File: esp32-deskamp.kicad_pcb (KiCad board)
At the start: 2 copper layers, 140.2 x 66.5 mm, 39 parts, among them J1 INPUT 00, J10 ADDITIONAL GPIO, J2 INPUT 01, J3 MUTE, J4 SLEEP, J5 PRE OUT, J6 LFE OUT, J7 INPUT SELECT, J8 MOTOR, J9 12V IN, K1 INPUT 00, K2 INPUT 01, K3 AMP MUTE, K4 AMP SLEEP, U1 ESP32 D1 MINI, U2 TSR 1-2433, U3 L9110, U4 ULN2003A

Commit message: DRC checks
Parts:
- removed ? (x6): , 
- removed the REF** at (227.2, 96.5)
- removed the REF** at (106.8, 37.2)
- removed the REF** at (227.2, 57.8)
- removed the REF** at (106.8, 96.5)
- added REF**: MountingHole_3.2mm_M3_DIN965_Pad_TopOnly, MountingHole:MountingHole_3.2mm_M3_DIN965_Pad_TopOnly, F.Cu at (227.2, 96.2)
- added REF**: MountingHole_3.2mm_M3_DIN965_Pad_TopOnly, MountingHole:MountingHole_3.2mm_M3_DIN965_Pad_TopOnly, F.Cu at (227.2, 57.5)
- added REF**: MountingHole_3.2mm_M3_DIN965_Pad_TopOnly, MountingHole:MountingHole_3.2mm_M3_DIN965_Pad_TopOnly, F.Cu at (95.8, 96.0)
- added REF**: MountingHole_3.2mm_M3_DIN965_Pad_TopOnly, MountingHole:MountingHole_3.2mm_M3_DIN965_Pad_TopOnly, F.Cu at (95.8, 38.2)
- moved J9 8.50 mm to (107.0, 39.5)
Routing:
- net +12V: track 175.0 -> 181.9 mm

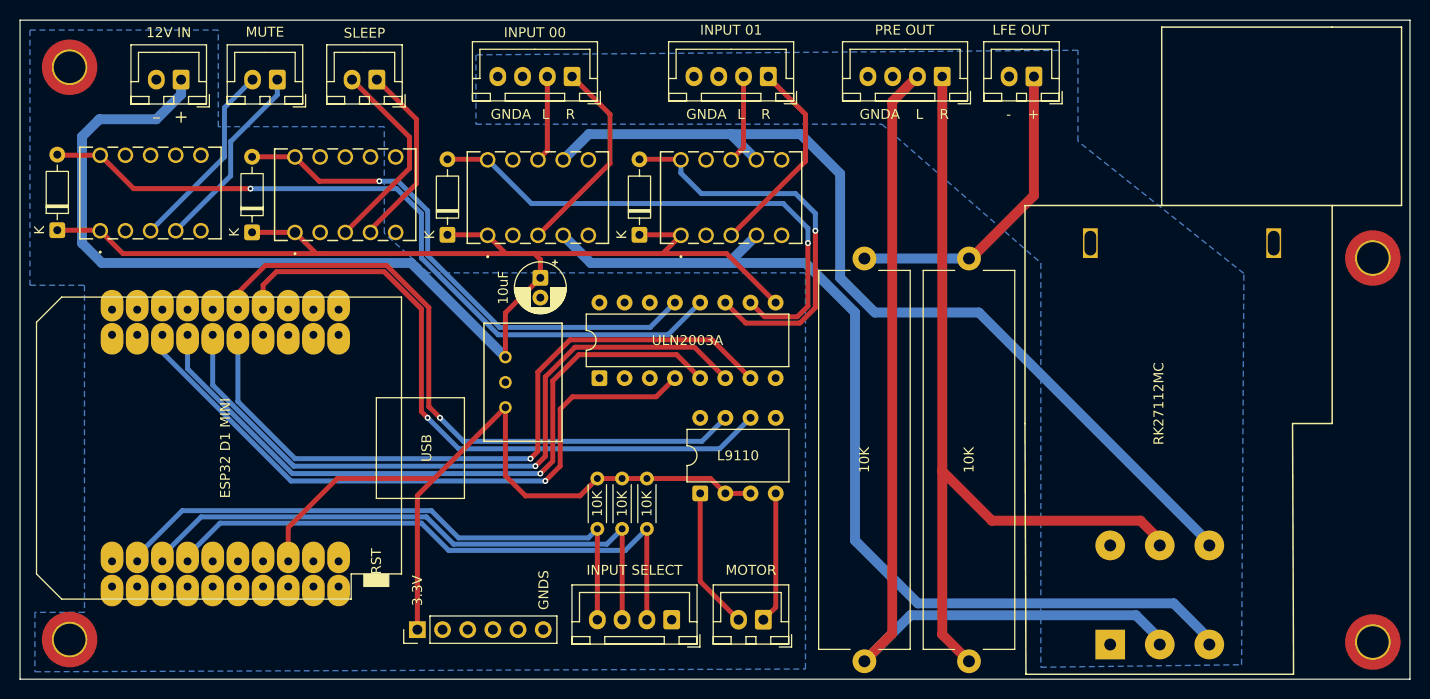
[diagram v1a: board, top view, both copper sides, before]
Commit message: Bump relays to 1mm track
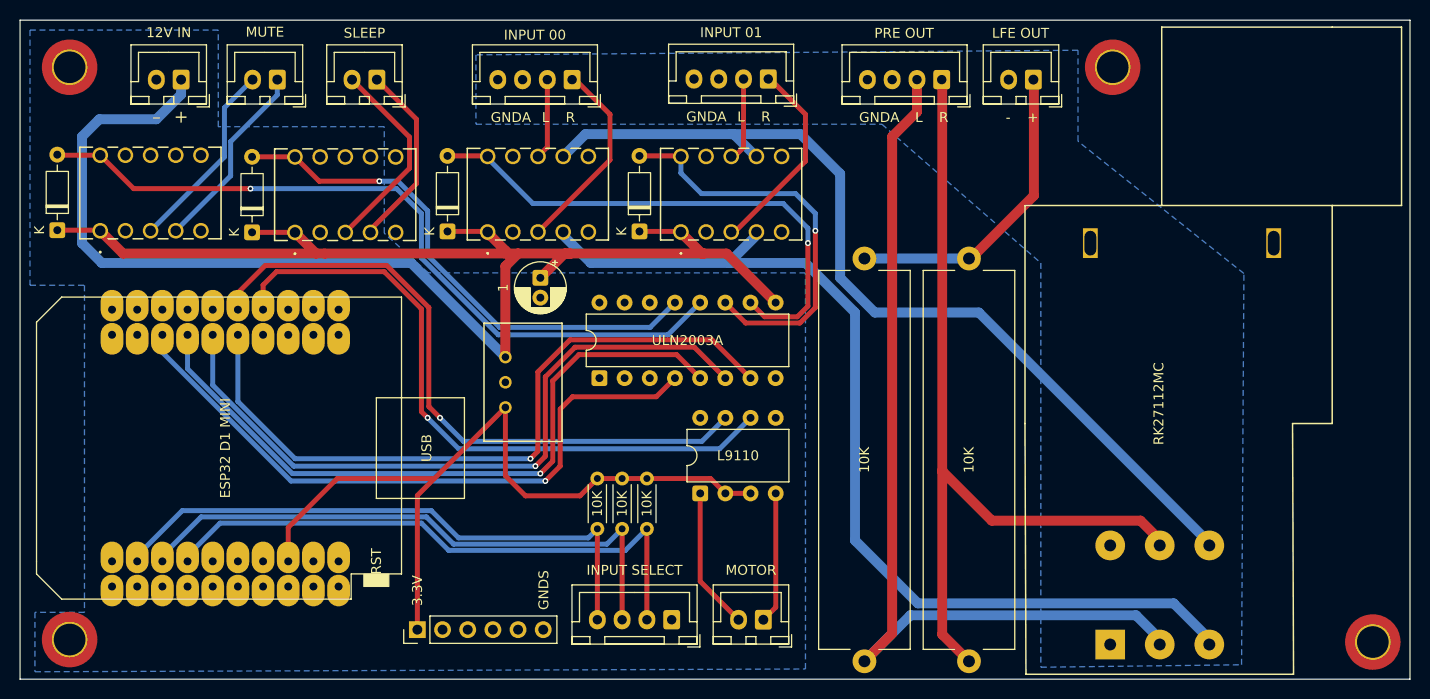
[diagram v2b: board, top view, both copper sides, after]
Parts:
- C1: value 10uF -> 1
- moved REF** 32.6 mm to (201.0, 38.2)
- moved D1 0.34 mm to (133.9, 54.8)
- moved D2 0.34 mm to (153.2, 54.8)
- moved K1 0.34 mm to (137.9, 54.9)
- moved K2 0.34 mm to (157.4, 54.9)
- moved J5 0.32 mm to (183.8, 39.5)
- moved J6 0.32 mm to (193.0, 39.5)
- moved J1 0.31 mm to (146.5, 39.5)
- moved J2 0.25 mm to (166.2, 39.4)
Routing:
- net +12V: track 181.9 -> 185.3 mm

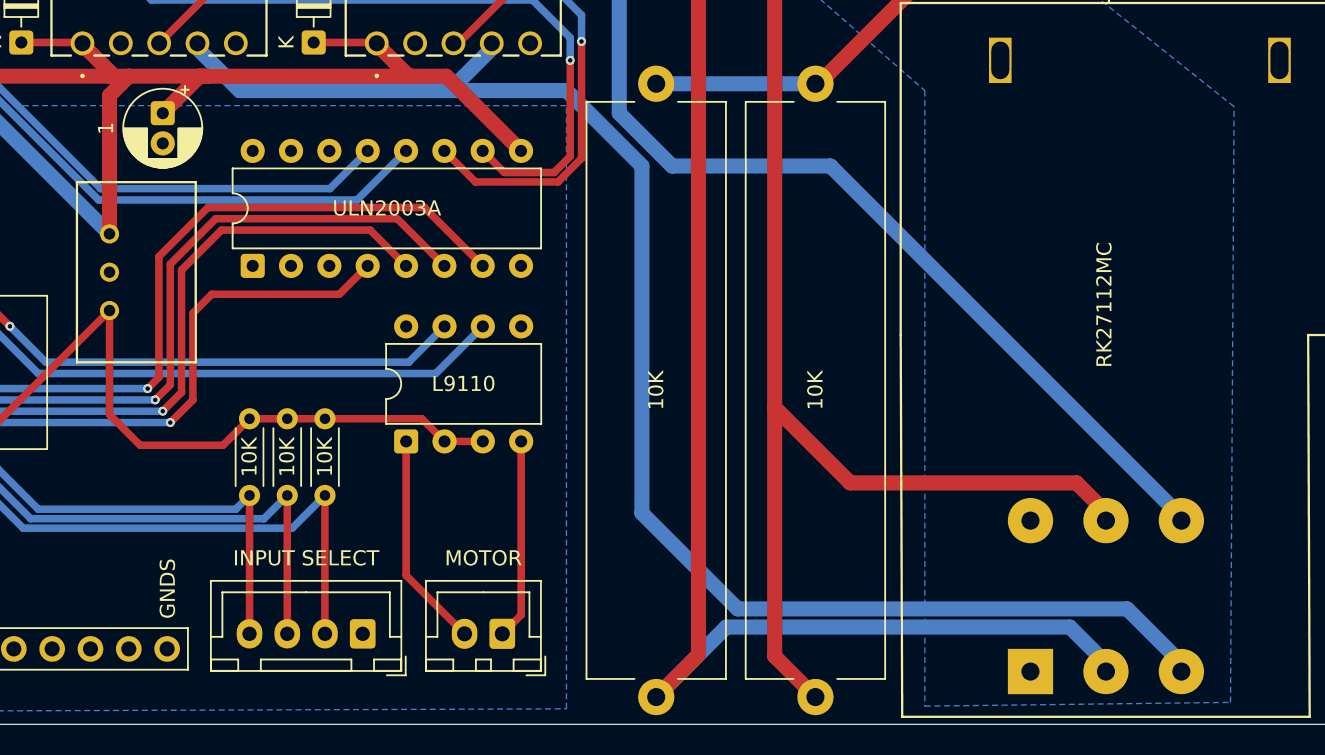
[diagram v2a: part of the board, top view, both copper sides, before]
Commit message: Name nets
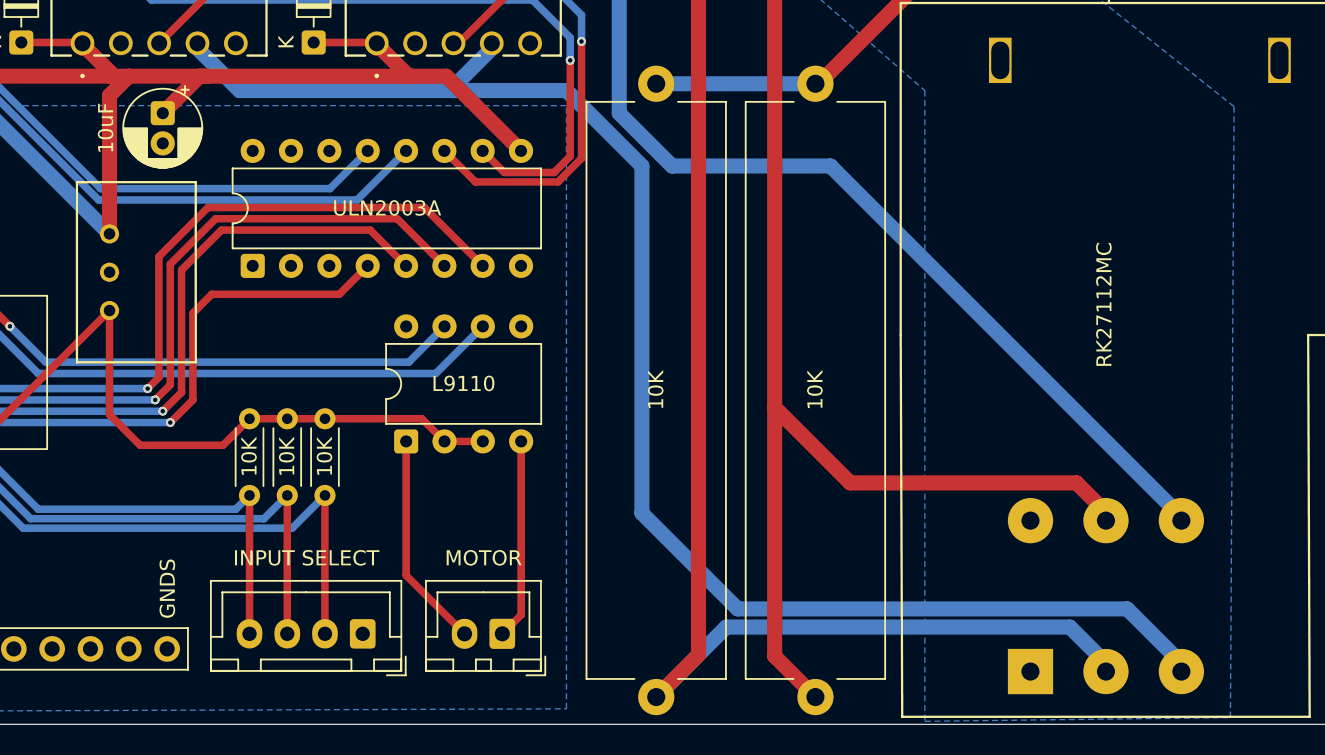
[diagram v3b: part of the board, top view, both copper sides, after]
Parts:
- C1: value 1 -> 10uF
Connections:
- J10 pad 2: unconnected-(J10-Pin_2-Pad2) -> IO1
- J10 pad 3: unconnected-(J10-Pin_3-Pad3) -> IO2
- J10 pad 4: unconnected-(J10-Pin_4-Pad4) -> IO3
- J10 pad 5: unconnected-(J10-Pin_5-Pad5) -> IO4
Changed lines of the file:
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@@
 	(net 73 "unconnected-(U1-IO_39{slash}SVN-Pad5)")
 	(net 74 "unconnected-(U1-CLK-Pad40)")
-	(net 75 "unconnected-(J10-Pin_2-Pad2)")
-	(net 76 "unconnected-(J10-Pin_4-Pad4)")
-	(net 77 "unconnected-(J10-Pin_5-Pad5)")
-	(net 78 "unconnected-(J10-Pin_3-Pad3)")
+	(net 75 "IO3")
+	(net 76 "IO2")
+	(net 77 "IO4")
+	(net 78 "IO1")
 	(net 79 "Net-(J5-Pin_1)")
 	(net 80 "Net-(J5-Pin_2)")
@@
 			)
 		)
-		(property "Value" "1"
+		(property "Value" "10uF"
 			(at 1 3.75 90)
 			(layer "F.SilkS")
@@
 			(layers "*.Cu" "*.Mask")
 			(remove_unused_layers no)
-			(net 75 "unconnected-(J10-Pin_2-Pad2)")
+			(net 78 "IO1")
 			(pinfunction "Pin_2")
 			(pintype "passive")
@@
 			(layers "*.Cu" "*.Mask")
 			(remove_unused_layers no)
-			(net 78 "unconnected-(J10-Pin_3-Pad3)")
+			(net 76 "IO2")
 			(pinfunction "Pin_3")
 			(pintype "passive")
@@
 			(layers "*.Cu" "*.Mask")
 			(remove_unused_layers no)
-			(net 76 "unconnected-(J10-Pin_4-Pad4)")
+			(net 75 "IO3")
 			(pinfunction "Pin_4")
 			(pintype "passive")
@@
 			(layers "*.Cu" "*.Mask")
 			(remove_unused_layers no)
-			(net 77 "unconnected-(J10-Pin_5-Pad5)")
+			(net 77 "IO4")
 			(pinfunction "Pin_5")
 			(pintype "passive")
@@
 		(polygon
 			(pts
-				(xy 136.75 37.000005) (xy 136.75 44) (xy 177.713636 44) (xy 193.75 58) (xy 193.75 98.793209) (xy 214.004232 98.543157)
+				(xy 136.75 37.000005) (xy 136.75 44) (xy 177.713636 44) (xy 193.75 58) (xy 193.75 99.799381) (xy 213.998207 99.549403)
 				(xy 214.240641 59.062861) (xy 197.5 45.722663) (xy 197.5 36.534488)
 			)

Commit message: Move cap
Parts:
- moved C1 1.00 mm to (144.2, 59.5)
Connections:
- J10 pad 1: +3V3 -> IO1
- J10 pad 2: IO1 -> IO2
- J10 pad 3: IO2 -> IO3
- J10 pad 4: IO3 -> IO4
- J10 pad 5: IO4 -> +3V3
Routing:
- net +3V3: track 80.1 -> 82.7 mm
- net Relay2: vias 1 -> 0
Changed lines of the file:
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@@
 	(footprint "Capacitor_THT:CP_Radial_D5.0mm_P2.00mm"
 		(layer "F.Cu")
-		(at 143.25 59.5 -90)
+		(at 144.25 59.5 -90)
 		(descr "CP, Radial series, Radial, pin pitch=2.00mm, diameter=5mm, height=7mm, Electrolytic Capacitor")
 		(tags "CP Radial series Radial pin pitch 2.00mm diameter 5mm height 7mm Electrolytic Capacitor")
@@
 			(layers "*.Cu" "*.Mask")
 			(remove_unused_layers no)
-			(net 45 "+3V3")
+			(net 78 "IO1")
 			(pinfunction "Pin_1")
 			(pintype "passive")
@@
 			(layers "*.Cu" "*.Mask")
 			(remove_unused_layers no)
-			(net 78 "IO1")
+			(net 76 "IO2")
 			(pinfunction "Pin_2")
 			(pintype "passive")
@@
 			(layers "*.Cu" "*.Mask")
 			(remove_unused_layers no)
-			(net 76 "IO2")
+			(net 75 "IO3")
 			(pinfunction "Pin_3")
 			(pintype "passive")
@@
 			(layers "*.Cu" "*.Mask")
 			(remove_unused_layers no)
-			(net 75 "IO3")
+			(net 77 "IO4")
 			(pinfunction "Pin_4")
 			(pintype "passive")
@@
 			(layers "*.Cu" "*.Mask")
 			(remove_unused_layers no)
-			(net 77 "IO4")
+			(net 45 "+3V3")
 			(pinfunction "Pin_5")
 			(pintype "passive")
@@
 	)
 	(gr_text "3.3V"
-		(at 130.84 89.5 90)
+		(at 141 89.75 90)
 		(layer "F.SilkS")
 		(effects
@@
 	)
 	(segment
+		(start 144.25 59.05)
+		(end 146.25 57.05)
+		(width 1)
+		(layer "F.Cu")
+		(net 2)
+	)
+	(segment
 		(start 145.7 57.05)
 		(end 146.25 57.05)
@@
 	)
 	(segment
+		(start 144.25 59.5)
+		(end 144.25 59.05)
+		(width 1)
+		(layer "F.Cu")
+		(net 2)
+	)
+	(segment
 		(start 98.84 54.75)
 		(end 101.14 57.05)
@@
 	)
 	(segment
-		(start 143.25 59.5)
-		(end 145.7 57.05)
-		(width 1)
-		(layer "F.Cu")
-		(net 2)
-	)
-	(segment
 		(start 138.1979 55.2131)
 		(end 139.7696 56.7848)
@@
 	)
 	(segment
-		(start 111.372 47.298)
-		(end 111.372 42.3353)
+		(start 111.872 46.798)
+		(end 111.872 41.8353)
 		(width 0.5)
-		(layer "B.Cu")
+		(layer "F.Cu")
 		(net 25)
 	)
 	(segment
-		(start 111.372 42.3353)
-		(end 114.2073 39.5)
+		(start 103.92 54.75)
+		(end 111.872 46.798)
 		(width 0.5)
-		(layer "B.Cu")
+		(layer "F.Cu")
 		(net 25)
 	)
 	(segment
-		(start 103.92 54.75)
-		(end 111.372 47.298)
+		(start 111.872 41.8353)
+		(end 114.2073 39.5)
 		(width 0.5)
-		(layer "B.Cu")
+		(layer "F.Cu")
 		(net 25)
 	)
 	(segment
-		(start 112 49.21)
-		(end 112 45.75)
+		(start 116.7073 39.5)
+		(end 112.5 43.7073)
 		(width 0.5)
-		(layer "B.Cu")
+		(layer "F.Cu")
 		(net 29)
 	)
 	(segment
-		(start 116.7073 39.5)
-		(end 116.7073 41.0427)
+		(start 106.46 53.54)
+		(end 106.46 54.75)
 		(width 0.5)
-		(layer "B.Cu")
+		(layer "F.Cu")
 		(net 29)
 	)
 	(segment
-		(start 106.46 54.75)
-		(end 112 49.21)
+		(start 112.5 47.5)
+		(end 106.46 53.54)
 		(width 0.5)
-		(layer "B.Cu")
+		(layer "F.Cu")
 		(net 29)
 	)
 	(segment
-		(start 112 45.75)
-		(end 116.7073 41.0427)
+		(start 112.5 43.7073)
+		(end 112.5 47.5)
 		(width 0.5)
-		(layer "B.Cu")
+		(layer "F.Cu")
 		(net 29)
 	)
@@
 	)
 	(segment
-		(start 130.84 95)
-		(end 130.84 81.462)
-		(width 0.5)
-		(layer "F.Cu")
-		(net 45)
-	)
-	(segment
 		(start 117.81 84.69)
 		(end 117.81 88.11)
@@
 	)
 	(segment
+		(start 141 87.75)
+		(end 149 79.75)
+		(width 0.5)
+		(layer "F.Cu")
+		(net 45)
+	)
+	(segment
 		(start 139.722 72.58)
 		(end 139.722 79.472)
@@
 	)
 	(segment
-		(start 132.552 79.75)
-		(end 130.84 81.462)
+		(start 141 95)
+		(end 141 87.75)
 		(width 0.5)
 		(layer "F.Cu")
@@
 	)
 	(segment
-		(start 114 50.5)
-		(end 102.21 50.5)
+		(start 98.84 47.13)
+		(end 94.5673 47.13)
 		(width 0.5)
 		(layer "F.Cu")
@@
 	)
 	(segment
-		(start 102.21 50.5)
-		(end 98.84 47.13)
+		(start 159.37 62)
+		(end 156.12 65.25)
 		(width 0.5)
-		(layer "F.Cu")
+		(layer "B.Cu")
 		(net 88)
 	)
 	(segment
-		(start 98.84 47.13)
-		(end 94.5673 47.13)
+		(start 156.12 65.25)
+		(end 139 65.25)
 		(width 0.5)
-		(layer "F.Cu")
-		(net 88)
-	)
-	(via
-		(at 114 50.5)
-		(size 0.6)
-		(drill 0.3)
-		(layers "F.Cu" "B.Cu")
+		(layer "B.Cu")
 		(net 88)
 	)
 	(segment
-		(start 114 50.5)
-		(end 128.75 50.5)
+		(start 139 65.25)
+		(end 131.25 57.5)
 		(width 0.5)
 		(layer "B.Cu")
@@
 	(segment
 		(start 128.75 50.5)
-		(end 131.25 53)
+		(end 102.21 50.5)
 		(width 0.5)
 		(layer "B.Cu")
@@
 	(segment
 		(start 131.25 57.5)
-		(end 139 65.25)
-		(width 0.5)
-		(layer "B.Cu")
-		(net 88)
-	)
-	(segment
-		(start 139 65.25)
-		(end 156.12 65.25)
+		(end 131.25 53)
 		(width 0.5)
 		(layer "B.Cu")
@@
 	)
 	(segment
-		(start 156.12 65.25)
-		(end 159.37 62)
+		(start 131.25 53)
+		(end 128.75 50.5)
 		(width 0.5)
 		(layer "B.Cu")
@@
 	)
 	(segment
-		(start 131.25 53)
-		(end 131.25 57.5)
+		(start 102.21 50.5)
+		(end 98.84 47.13)
 		(width 0.5)
 		(layer "B.Cu")
@@
 			(pts
 				(xy 91.75 34.5) (xy 91.75 60.25) (xy 97.25 60.25) (xy 97.25 93.25) (xy 92.25 93.25) (xy 92.25 99.25)
-				(xy 170 98.969772) (xy 170 59) (xy 131.944445 59) (xy 127.5 55) (xy 127.5 44.25) (xy 110.75 44.25)
+				(xy 170 98.969772) (xy 170 59) (xy 131.944445 59) (xy 127.5 55) (xy 127.5 51.25) (xy 110.75 51.25)
 				(xy 110.75 34.5)
 			)

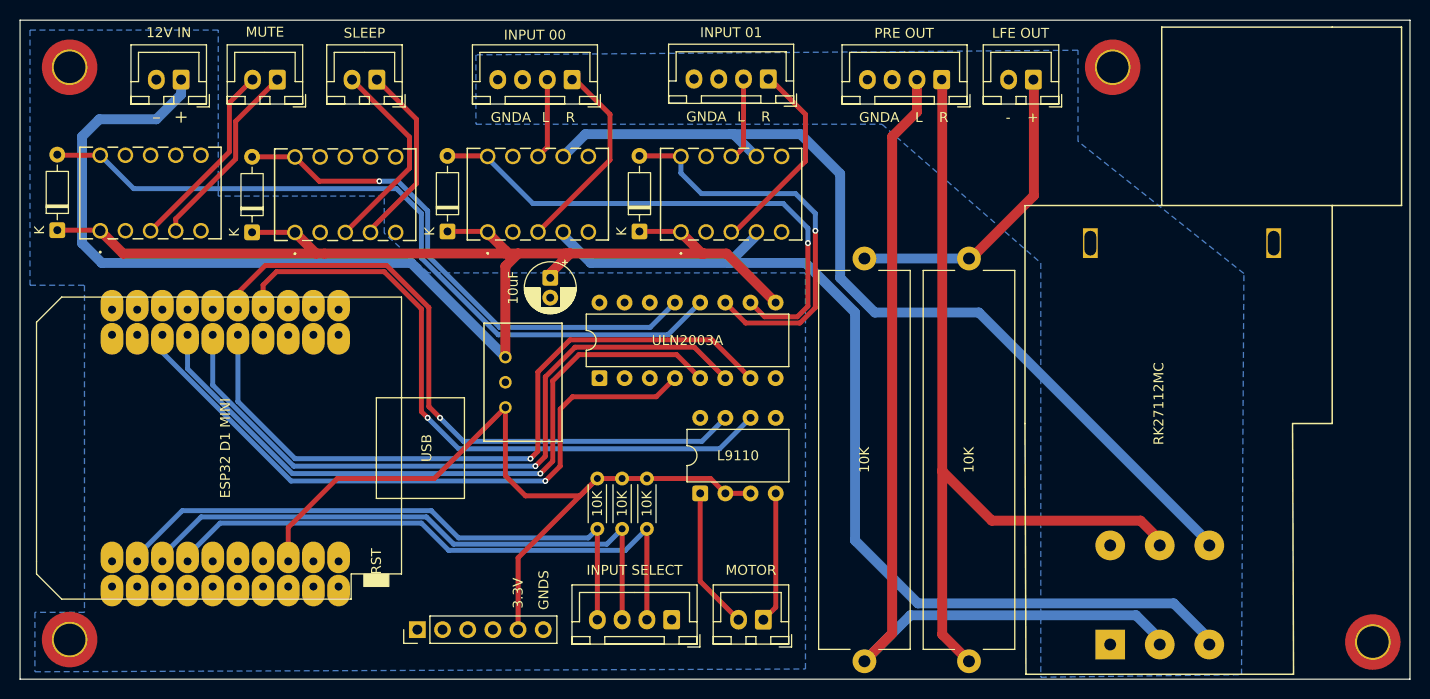
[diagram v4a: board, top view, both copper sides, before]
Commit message: Resolve DRC warnings
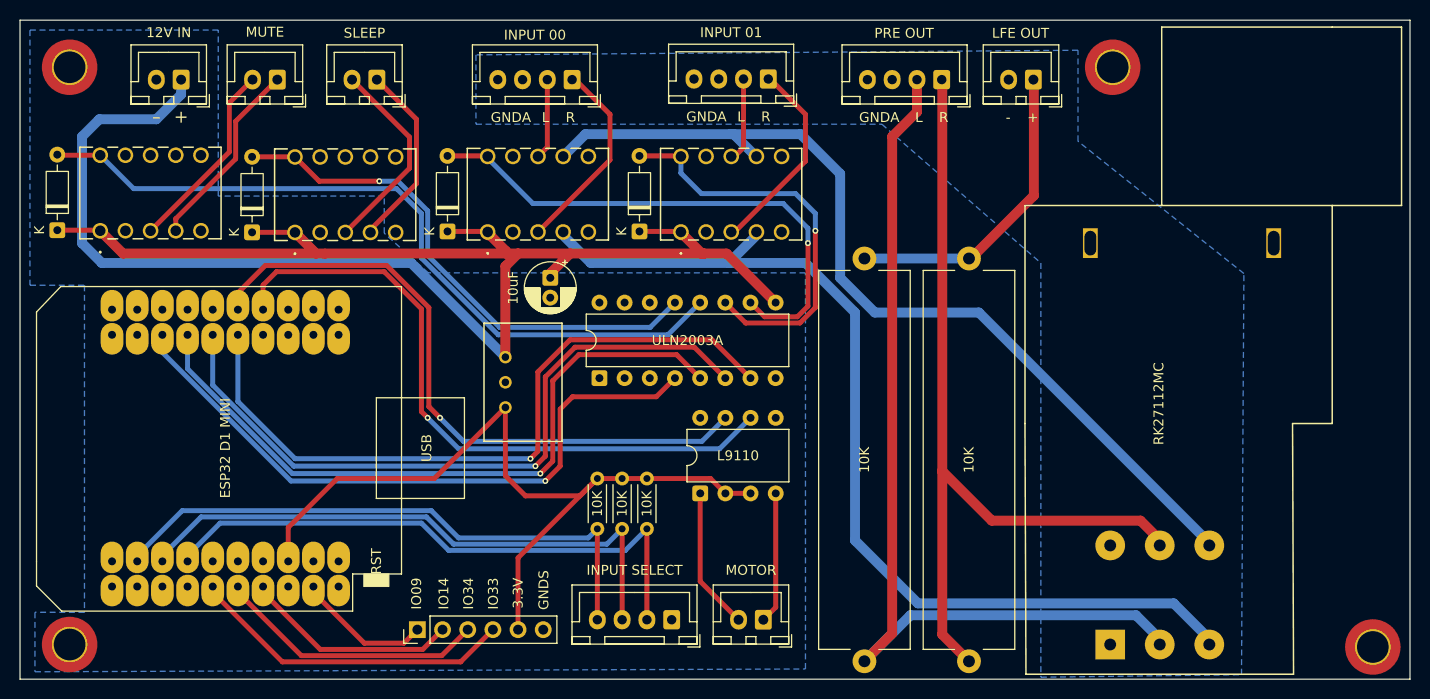
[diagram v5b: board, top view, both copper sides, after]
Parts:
- moved REF** 0.50 mm to (227.2, 96.8)
- moved REF** 0.50 mm to (95.8, 96.5)
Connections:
- U1 pad 11: unconnected-(U1-IO_34-Pad11) -> IO3
- U1 pad 13: unconnected-(U1-IO_14/TMS-Pad13) -> IO2
- U1 pad 17: unconnected-(U1-IO_09/SD2-Pad17) -> IO1
- U1 pad 9: unconnected-(U1-IO_33-Pad9) -> IO4
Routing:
- net IO4: track 0.00 -> 32.5 mm
- net IO3: track 0.00 -> 26.9 mm
- net IO2: track 0.00 -> 21.3 mm
- net IO1: track 0.00 -> 13.2 mm
- net +12V: track 185.1 -> 184.6 mm
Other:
- board text added: "IO09"
- board text added: "IO14"
- board text added: "IO33"
- board text added: "IO34"
